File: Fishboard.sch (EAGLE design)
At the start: 21 parts, among them J3 B1, J4 B2, J5 B3, J7 B4, Q1 FQP30N06L, Q2 FQP30N06L

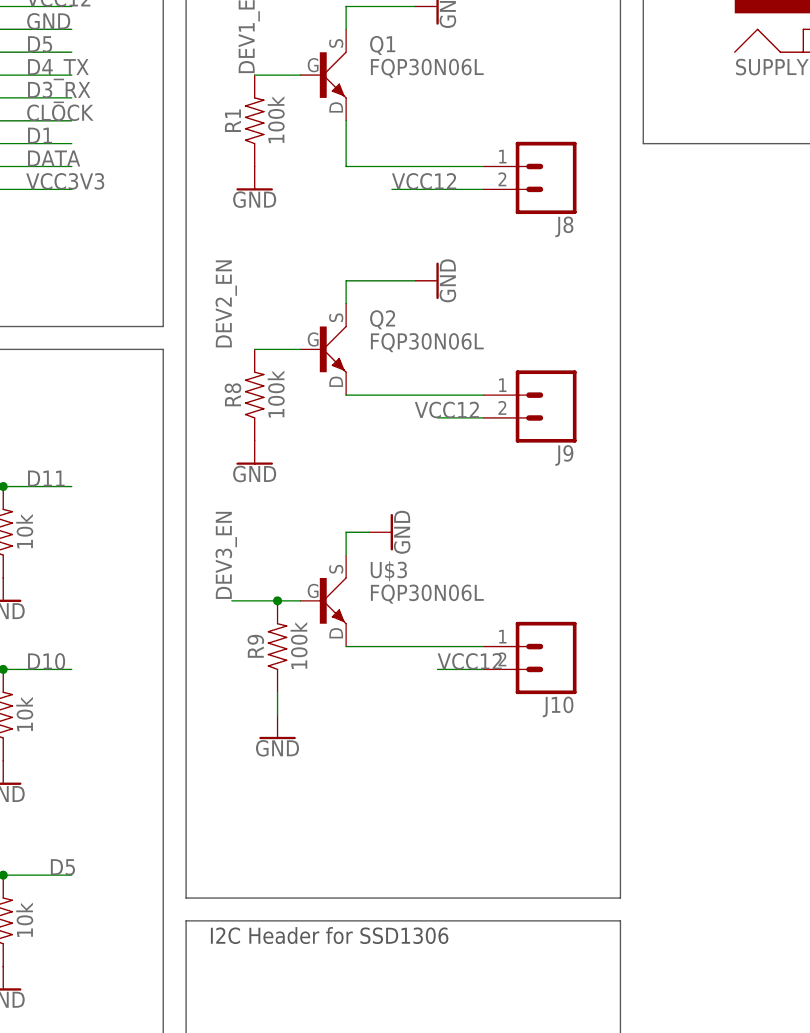
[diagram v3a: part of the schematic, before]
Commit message: Moved Open Source Hardware logo to bottom of board. Added flyback diodes.
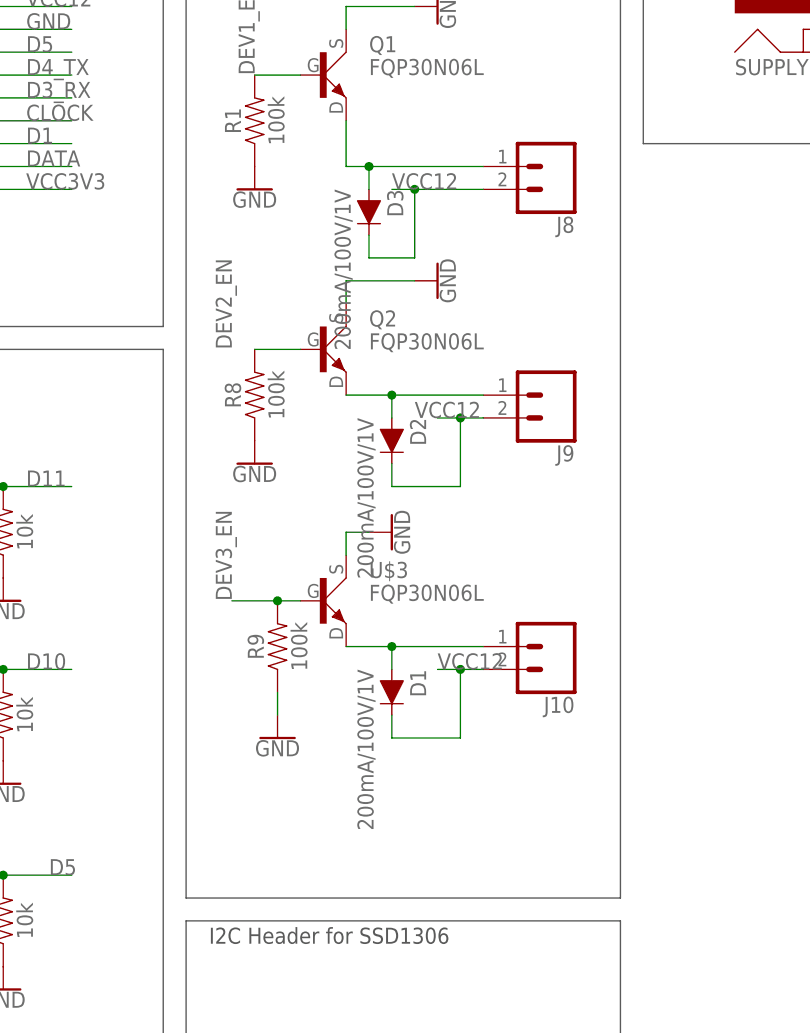
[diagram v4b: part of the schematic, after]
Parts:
- added D1, D2, D3: 200mA/100V/1V, SparkFun-DiscreteSemi:DIODE-KIT
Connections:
- net N$1: now also D2.A
- net N$2: now also D3.A
- net N$4: now also D1.A
- net VCC12: now also D1.C, D2.C, D3.C
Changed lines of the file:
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@@
 <part name="Q2" library="fishlib" deviceset="FQP30N06L" device=""/>
 <part name="U$3" library="fishlib" deviceset="FQP30N06L" device=""/>
+<part name="D1" library="SparkFun-DiscreteSemi" deviceset="DIODE" device="-KIT" value="200mA/100V/1V"/>
+<part name="D2" library="SparkFun-DiscreteSemi" deviceset="DIODE" device="-KIT" value="200mA/100V/1V"/>
+<part name="D3" library="SparkFun-DiscreteSemi" deviceset="DIODE" device="-KIT" value="200mA/100V/1V"/>
 </parts>
 <sheets>
@@
 <instance part="Q2" gate="G$1" x="76.2" y="45.72"/>
 <instance part="U$3" gate="G$1" x="76.2" y="17.78"/>
+<instance part="D1" gate="G$1" x="83.82" y="7.62" rot="R270"/>
+<instance part="D2" gate="G$1" x="83.82" y="35.56" rot="R270"/>
+<instance part="D3" gate="G$1" x="81.28" y="60.96" rot="R270"/>
 </instances>
 <busses>
@@
 <label x="83.82" y="63.5" size="1.778" layer="95"/>
 <pinref part="J8" gate="G$1" pin="2"/>
-<wire x1="93.98" y1="63.5" x2="83.82" y2="63.5" width="0.1524" layer="91"/>
+<wire x1="93.98" y1="63.5" x2="86.36" y2="63.5" width="0.1524" layer="91"/>
+<pinref part="D3" gate="G$1" pin="C"/>
+<wire x1="86.36" y1="63.5" x2="83.82" y2="63.5" width="0.1524" layer="91"/>
+<wire x1="81.28" y1="58.42" x2="81.28" y2="55.88" width="0.1524" layer="91"/>
+<wire x1="81.28" y1="55.88" x2="86.36" y2="55.88" width="0.1524" layer="91"/>
+<wire x1="86.36" y1="55.88" x2="86.36" y2="63.5" width="0.1524" layer="91"/>
+<junction x="86.36" y="63.5"/>
 </segment>
 <segment>
@@
 <label x="86.36" y="38.1" size="1.778" layer="95"/>
 <pinref part="J9" gate="G$1" pin="2"/>
-<wire x1="93.98" y1="38.1" x2="88.9" y2="38.1" width="0.1524" layer="91"/>
-</segment>
-<segment>
-<wire x1="93.98" y1="10.16" x2="88.9" y2="10.16" width="0.1524" layer="91"/>
+<wire x1="93.98" y1="38.1" x2="91.44" y2="38.1" width="0.1524" layer="91"/>
+<junction x="91.44" y="38.1"/>
+<wire x1="91.44" y1="38.1" x2="88.9" y2="38.1" width="0.1524" layer="91"/>
+<pinref part="D2" gate="G$1" pin="C"/>
+<wire x1="83.82" y1="33.02" x2="83.82" y2="30.48" width="0.1524" layer="91"/>
+<wire x1="83.82" y1="30.48" x2="91.44" y2="30.48" width="0.1524" layer="91"/>
+<wire x1="91.44" y1="30.48" x2="91.44" y2="38.1" width="0.1524" layer="91"/>
+</segment>
+<segment>
+<wire x1="93.98" y1="10.16" x2="91.44" y2="10.16" width="0.1524" layer="91"/>
 <label x="88.9" y="10.16" size="1.778" layer="95"/>
 <pinref part="J10" gate="G$1" pin="2"/>
+<junction x="91.44" y="10.16"/>
+<wire x1="91.44" y1="10.16" x2="88.9" y2="10.16" width="0.1524" layer="91"/>
+<pinref part="D1" gate="G$1" pin="C"/>
+<wire x1="83.82" y1="5.08" x2="83.82" y2="2.54" width="0.1524" layer="91"/>
+<wire x1="83.82" y1="2.54" x2="91.44" y2="2.54" width="0.1524" layer="91"/>
+<wire x1="91.44" y1="2.54" x2="91.44" y2="10.16" width="0.1524" layer="91"/>
 </segment>
 </net>
@@
 <wire x1="78.74" y1="71.12" x2="78.74" y2="66.04" width="0.1524" layer="91"/>
 <pinref part="J8" gate="G$1" pin="1"/>
-<wire x1="78.74" y1="66.04" x2="93.98" y2="66.04" width="0.1524" layer="91"/>
+<wire x1="78.74" y1="66.04" x2="81.28" y2="66.04" width="0.1524" layer="91"/>
+<pinref part="D3" gate="G$1" pin="A"/>
+<wire x1="81.28" y1="66.04" x2="93.98" y2="66.04" width="0.1524" layer="91"/>
+<wire x1="81.28" y1="66.04" x2="81.28" y2="63.5" width="0.1524" layer="91"/>
+<junction x="81.28" y="66.04"/>
 </segment>
 </net>
@@
 <pinref part="J9" gate="G$1" pin="1"/>
 <pinref part="Q2" gate="G$1" pin="2"/>
-<wire x1="93.98" y1="40.64" x2="78.74" y2="40.64" width="0.1524" layer="91"/>
+<wire x1="93.98" y1="40.64" x2="83.82" y2="40.64" width="0.1524" layer="91"/>
+<junction x="83.82" y="40.64"/>
+<wire x1="83.82" y1="40.64" x2="78.74" y2="40.64" width="0.1524" layer="91"/>
+<pinref part="D2" gate="G$1" pin="A"/>
+<wire x1="83.82" y1="40.64" x2="83.82" y2="38.1" width="0.1524" layer="91"/>
 </segment>
 </net>
@@
 <pinref part="U$3" gate="G$1" pin="2"/>
 <pinref part="J10" gate="G$1" pin="1"/>
-<wire x1="78.74" y1="12.7" x2="93.98" y2="12.7" width="0.1524" layer="91"/>
-</segment>
-</net>
+<wire x1="78.74" y1="12.7" x2="83.82" y2="12.7" width="0.1524" layer="91"/>
+<junction x="83.82" y="12.7"/>
+<wire x1="83.82" y1="12.7" x2="93.98" y2="12.7" width="0.1524" layer="91"/>
+<pinref part="D1" gate="G$1" pin="A"/>
+<wire x1="83.82" y1="12.7" x2="83.82" y2="10.16" width="0.1524" layer="91"/>
+</segment>
+</net>

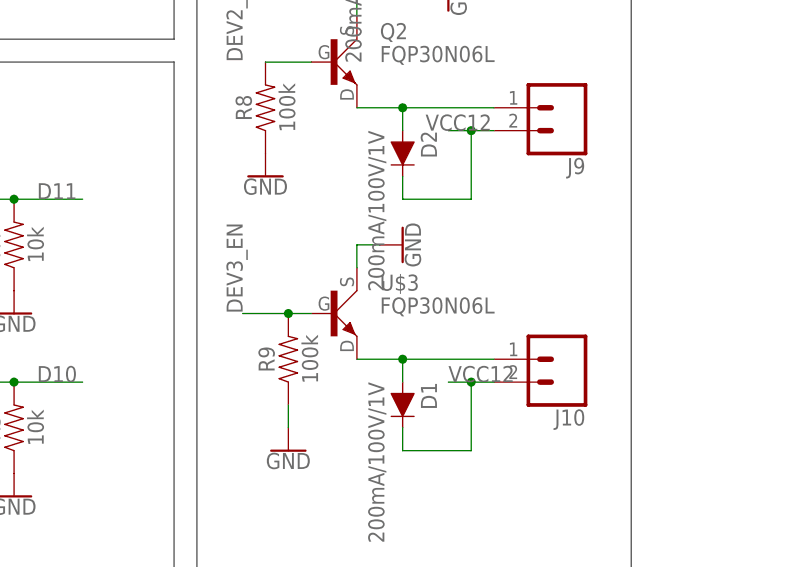
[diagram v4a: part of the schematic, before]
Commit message: Change the net for the gndplane-connecting vias to GND. Renamed a FET to Q3 instead of U$3.
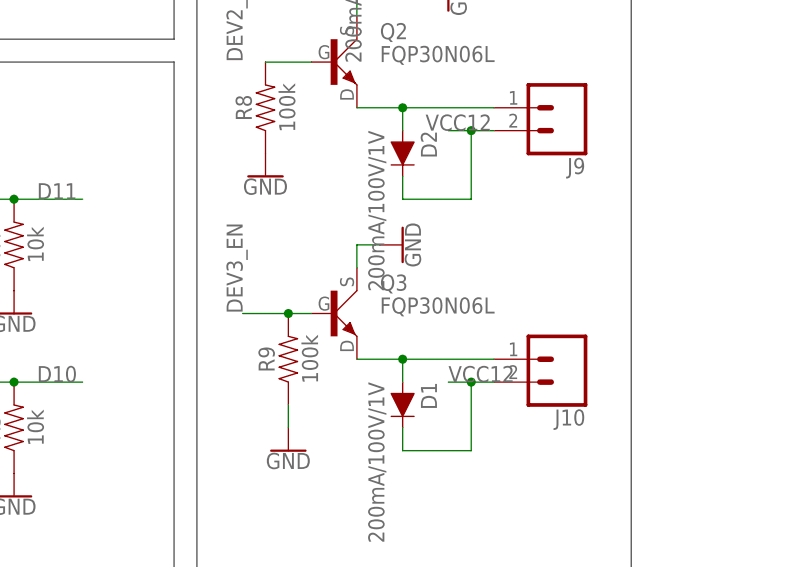
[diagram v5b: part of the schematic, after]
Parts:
- renumbered U$3 to Q3
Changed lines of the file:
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@@
 <part name="Q1" library="fishlib" deviceset="FQP30N06L" device=""/>
 <part name="Q2" library="fishlib" deviceset="FQP30N06L" device=""/>
-<part name="U$3" library="fishlib" deviceset="FQP30N06L" device=""/>
+<part name="Q3" library="fishlib" deviceset="FQP30N06L" device=""/>
 <part name="D1" library="SparkFun-DiscreteSemi" deviceset="DIODE" device="-KIT" value="200mA/100V/1V"/>
 <part name="D2" library="SparkFun-DiscreteSemi" deviceset="DIODE" device="-KIT" value="200mA/100V/1V"/>
@@
 <instance part="Q1" gate="G$1" x="76.2" y="76.2"/>
 <instance part="Q2" gate="G$1" x="76.2" y="45.72"/>
-<instance part="U$3" gate="G$1" x="76.2" y="17.78"/>
+<instance part="Q3" gate="G$1" x="76.2" y="17.78"/>
 <instance part="D1" gate="G$1" x="83.82" y="7.62" rot="R270"/>
 <instance part="D2" gate="G$1" x="83.82" y="35.56" rot="R270"/>
@@
 <segment>
 <pinref part="GND6" gate="1" pin="GND"/>
-<pinref part="U$3" gate="G$1" pin="3"/>
+<pinref part="Q3" gate="G$1" pin="3"/>
 <wire x1="81.28" y1="25.4" x2="78.74" y2="25.4" width="0.1524" layer="91"/>
 <wire x1="78.74" y1="25.4" x2="78.74" y2="22.86" width="0.1524" layer="91"/>
@@
 <wire x1="71.12" y1="17.78" x2="73.66" y2="17.78" width="0.1524" layer="91"/>
 <junction x="71.12" y="17.78"/>
-<pinref part="U$3" gate="G$1" pin="1"/>
+<pinref part="Q3" gate="G$1" pin="1"/>
 </segment>
 <segment>
@@
 <net name="N$4" class="0">
 <segment>
-<pinref part="U$3" gate="G$1" pin="2"/>
+<pinref part="Q3" gate="G$1" pin="2"/>
 <pinref part="J10" gate="G$1" pin="1"/>
 <wire x1="78.74" y1="12.7" x2="83.82" y2="12.7" width="0.1524" layer="91"/>
